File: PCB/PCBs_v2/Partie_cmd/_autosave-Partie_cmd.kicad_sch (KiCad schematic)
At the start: 54 parts, among them J1 Barrel_Jack, J2 Conn_01x04_Socket, J3 Conn_01x04_Socket, J4 Conn_01x11_Pin, J5 Conn_01x10_Pin, SW1 SW_MEC_5G, U1 ESP32-S3-DEVKITC-1-N8R2, U3 BU33SD5WG-TR, U4 XL1509-5.0

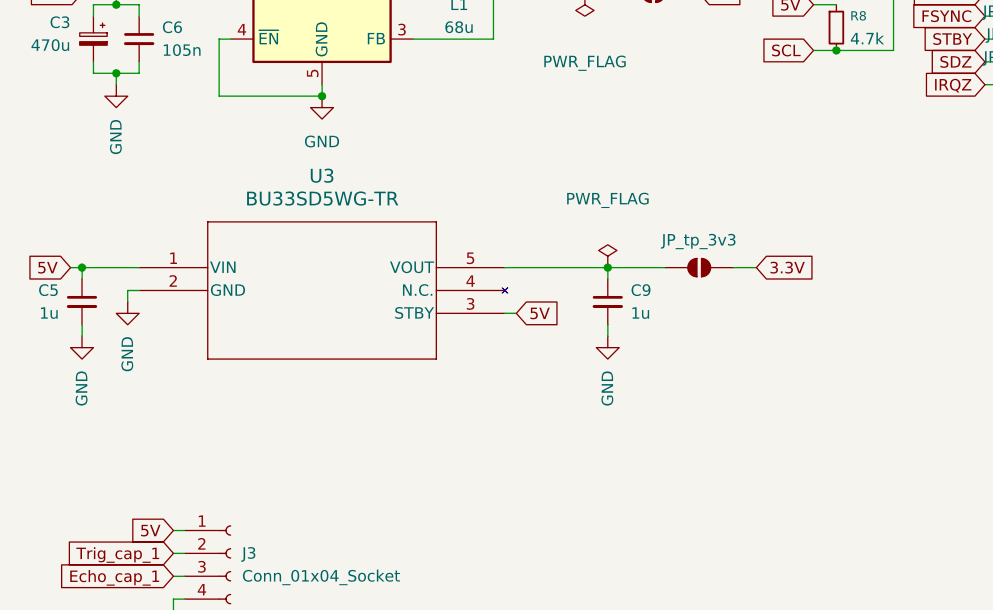
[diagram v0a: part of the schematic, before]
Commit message: pcb commande empruntes + debut routage
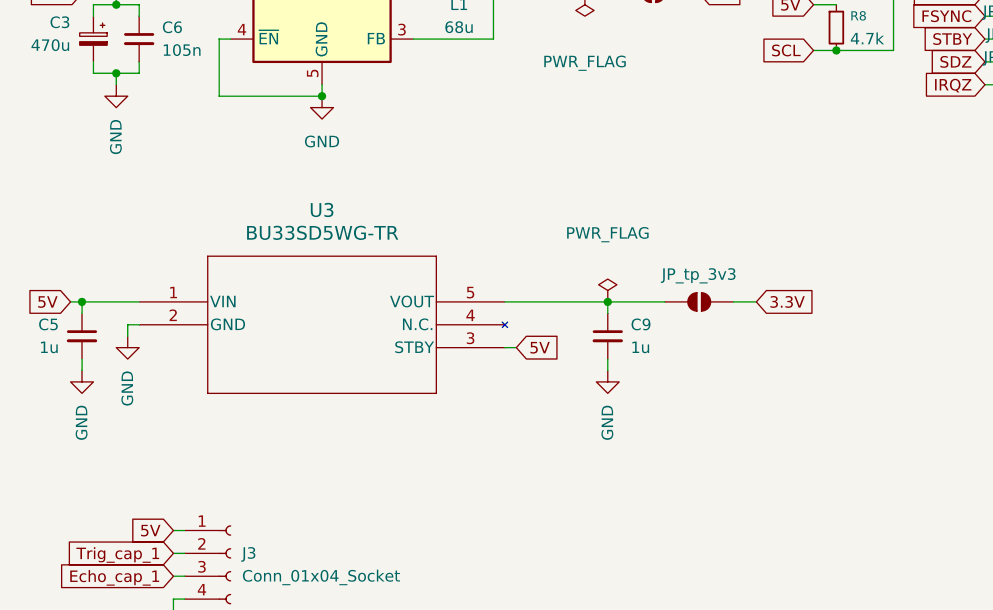
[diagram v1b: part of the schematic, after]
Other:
- moved on the sheet: C5, C9, JP_tp_3v3, U3
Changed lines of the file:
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@@
 	)
 	(junction
-		(at 40.64 99.06)
+		(at 40.64 102.87)
 		(diameter 0)
 		(color 0 0 0 0)
@@
 	)
 	(junction
-		(at 99.06 99.06)
+		(at 99.06 102.87)
 		(diameter 0)
 		(color 0 0 0 0)
@@
 	(wire
 		(pts
-			(xy 113.03 99.06) (xy 115.57 99.06)
+			(xy 113.03 102.87) (xy 115.57 102.87)
 		)
 		(stroke
@@
 	(wire
 		(pts
-			(xy 39.37 99.06) (xy 40.64 99.06)
+			(xy 39.37 102.87) (xy 40.64 102.87)
 		)
 		(stroke
@@
 	(wire
 		(pts
-			(xy 99.06 105.41) (xy 99.06 106.68)
+			(xy 99.06 109.22) (xy 99.06 110.49)
 		)
 		(stroke
@@
 	(wire
 		(pts
-			(xy 99.06 99.06) (xy 99.06 100.33)
+			(xy 99.06 102.87) (xy 99.06 104.14)
 		)
 		(stroke
@@
 	(wire
 		(pts
-			(xy 40.64 105.41) (xy 40.64 106.68)
+			(xy 40.64 109.22) (xy 40.64 110.49)
 		)
 		(stroke
@@
 	(wire
 		(pts
-			(xy 87.63 104.14) (xy 88.9 104.14)
+			(xy 87.63 107.95) (xy 88.9 107.95)
 		)
 		(stroke
@@
 	(wire
 		(pts
-			(xy 99.06 99.06) (xy 105.41 99.06)
+			(xy 99.06 102.87) (xy 105.41 102.87)
 		)
 		(stroke
@@
 	(wire
 		(pts
-			(xy 45.72 102.87) (xy 45.72 101.6)
+			(xy 45.72 106.68) (xy 45.72 105.41)
 		)
 		(stroke
@@
 	(wire
 		(pts
-			(xy 45.72 101.6) (xy 46.99 101.6)
+			(xy 45.72 105.41) (xy 46.99 105.41)
 		)
 		(stroke
@@
 	(wire
 		(pts
-			(xy 46.99 99.06) (xy 40.64 99.06)
+			(xy 46.99 102.87) (xy 40.64 102.87)
 		)
 		(stroke
@@
 	(wire
 		(pts
-			(xy 40.64 99.06) (xy 40.64 100.33)
+			(xy 40.64 102.87) (xy 40.64 104.14)
 		)
 		(stroke
@@
 	(wire
 		(pts
-			(xy 87.63 99.06) (xy 99.06 99.06)
+			(xy 87.63 102.87) (xy 99.06 102.87)
 		)
 		(stroke
@@
 	(global_label "5V"
 		(shape input)
-		(at 88.9 104.14 0)
+		(at 88.9 107.95 0)
 		(fields_autoplaced yes)
 		(effects
@@
 		)
 		(property "Intersheetrefs" "${INTERSHEET_REFS}"
-			(at 94.1833 104.14 0)
+			(at 94.1833 107.95 0)
 			(effects
 				(font
@@
 	(global_label "5V"
 		(shape input)
-		(at 39.37 99.06 180)
+		(at 39.37 102.87 180)
 		(fields_autoplaced yes)
 		(effects
@@
 		)
 		(property "Intersheetrefs" "${INTERSHEET_REFS}"
-			(at 34.0867 99.06 0)
+			(at 34.0867 102.87 0)
 			(effects
 				(font
@@
 	(global_label "3.3V"
 		(shape input)
-		(at 115.57 99.06 0)
+		(at 115.57 102.87 0)
 		(fields_autoplaced yes)
 		(effects
@@
 		)
 		(property "Intersheetrefs" "${INTERSHEET_REFS}"
-			(at 122.6676 99.06 0)
+			(at 122.6676 102.87 0)
 			(effects
 				(font
@@
 	(symbol
 		(lib_id "2025-09-19_12-39-26:BU33SD5WG-TR")
-		(at 46.99 99.06 0)
+		(at 46.99 102.87 0)
 		(unit 1)
 		(exclude_from_sim no)
@@
 		(fields_autoplaced yes)
 		(property "Reference" "U3"
-			(at 67.31 88.9 0)
+			(at 67.31 92.71 0)
 			(effects
 				(font
@@
 		)
 		(property "Value" "BU33SD5WG-TR"
-			(at 67.31 91.44 0)
+			(at 67.31 95.25 0)
 			(effects
 				(font
@@
 		)
 		(property "Footprint" "footprints:SSOP5_ROM-L"
-			(at 46.99 99.06 0)
+			(at 46.99 102.87 0)
 			(effects
 				(font
@@
 		)
 		(property "Datasheet" "BU33SD5WG-TR"
-			(at 46.99 99.06 0)
+			(at 46.99 102.87 0)
 			(effects
 				(font
@@
 		)
 		(property "Description" ""
-			(at 46.99 99.06 0)
+			(at 46.99 102.87 0)
 			(effects
 				(font
@@
 	(symbol
 		(lib_id "Device:C_Small")
-		(at 99.06 102.87 0)
+		(at 99.06 106.68 0)
 		(unit 1)
 		(exclude_from_sim no)
@@
 		(fields_autoplaced yes)
 		(property "Reference" "C9"
-			(at 101.6 101.6062 0)
+			(at 101.6 105.4162 0)
 			(effects
 				(font
@@
 		)
 		(property "Value" "1u"
-			(at 101.6 104.1462 0)
+			(at 101.6 107.9562 0)
 			(effects
 				(font
@@
 		)
 		(property "Footprint" "Capacitor_SMD:C_0603_1608Metric_Pad1.08x0.95mm_HandSolder"
-			(at 99.06 102.87 0)
+			(at 99.06 106.68 0)
 			(effects
 				(font
@@
 		)
 		(property "Datasheet" "~"
-			(at 99.06 102.87 0)
+			(at 99.06 106.68 0)
 			(effects
 				(font
@@
 		)
 		(property "Description" "Unpolarized capacitor, small symbol"
-			(at 99.06 102.87 0)
+			(at 99.06 106.68 0)
 			(effects
 				(font
@@
 	(symbol
 		(lib_id "power:PWR_FLAG")
-		(at 99.06 99.06 0)
+		(at 99.06 102.87 0)
 		(unit 1)
 		(exclude_from_sim no)
@@
 		(dnp no)
 		(property "Reference" "#FLG03"
-			(at 99.06 97.155 0)
+			(at 99.06 100.965 0)
 			(effects
 				(font
@@
 		)
 		(property "Value" "PWR_FLAG"
-			(at 99.06 91.44 0)
+			(at 99.06 95.25 0)
 			(effects
 				(font
@@
 		)
 		(property "Footprint" ""
-			(at 99.06 99.06 0)
+			(at 99.06 102.87 0)
 			(effects
 				(font
@@
 		)
 		(property "Datasheet" "~"
-			(at 99.06 99.06 0)
+			(at 99.06 102.87 0)
 			(effects
 				(font
@@
 		)
 		(property "Description" "Special symbol for telling ERC where power comes from"
-			(at 99.06 99.06 0)
+			(at 99.06 102.87 0)
 			(effects
 				(font
@@
 	(symbol
 		(lib_id "Jumper:SolderJumper_2_Open")
-		(at 109.22 99.06 0)
+		(at 109.22 102.87 0)
 		(unit 1)
 		(exclude_from_sim no)
@@
 		(dnp no)
 		(property "Reference" "JP_tp_3v3"
-			(at 109.22 96.012 0)
+			(at 109.22 99.822 0)
 			(effects
 				(font
@@
 		)
 		(property "Value" "SolderJumper_2_Open"
-			(at 109.22 95.25 0)
+			(at 109.22 99.06 0)
 			(effects
 				(font
@@
 		)
 		(property "Footprint" "Jumper:SolderJumper-2_P1.3mm_Open_TrianglePad1.0x1.5mm"
-			(at 109.22 99.06 0)
+			(at 109.22 102.87 0)
 			(effects
 				(font
@@
 		)
 		(property "Datasheet" "~"
-			(at 109.22 99.06 0)
+			(at 109.22 102.87 0)
 			(effects
 				(font
@@
 		)
 		(property "Description" "Solder Jumper, 2-pole, open"
-			(at 109.22 99.06 0)
+			(at 109.22 102.87 0)
 			(effects
 				(font
@@
 	(symbol
 		(lib_id "Device:C_Small")
-		(at 40.64 102.87 0)
+		(at 40.64 106.68 0)
 		(mirror y)
 		(unit 1)
@@
 		(dnp no)
 		(property "Reference" "C5"
-			(at 38.1 101.6062 0)
+			(at 38.1 105.4162 0)
 			(effects
 				(font
@@
 		)
 		(property "Value" "1u"
-			(at 38.1 104.1462 0)
+			(at 38.1 107.9562 0)
 			(effects
 				(font
@@
 		)
 		(property "Footprint" "Capacitor_SMD:C_0603_1608Metric_Pad1.08x0.95mm_HandSolder"
-			(at 40.64 102.87 0)
+			(at 40.64 106.68 0)
 			(effects
 				(font
@@
 		)
 		(property "Datasheet" "~"
-			(at 40.64 102.87 0)
+			(at 40.64 106.68 0)
 			(effects
 				(font
@@
 		)
 		(property "Description" "Unpolarized capacitor, small symbol"
-			(at 40.64 102.87 0)
+			(at 40.64 106.68 0)
 			(effects
 				(font
@@
 	(symbol
 		(lib_id "power:GND")
-		(at 45.72 102.87 0)
+		(at 45.72 106.68 0)
 		(unit 1)
 		(exclude_from_sim no)
@@
 		(fields_autoplaced yes)
 		(property "Reference" "#PWR08"
-			(at 45.72 109.22 0)
+			(at 45.72 113.03 0)
 			(effects
 				(font
@@
 		)
 		(property "Value" "GND"
-			(at 45.7201 106.68 90)
+			(at 45.7201 110.49 90)
 			(effects
 				(font
@@
 		)
 		(property "Footprint" ""
-			(at 45.72 102.87 0)
+			(at 45.72 106.68 0)
 			(effects
 				(font
@@
 		)
 		(property "Datasheet" ""
-			(at 45.72 102.87 0)
+			(at 45.72 106.68 0)
 			(effects
 				(font
@@
 		)
 		(property "Description" "Power symbol creates a global label with name \"GND\" , ground"
-			(at 45.72 102.87 0)
+			(at 45.72 106.68 0)
 			(effects
 				(font
@@
 	(symbol
 		(lib_id "power:GND")
-		(at 99.06 106.68 0)
+		(at 99.06 110.49 0)
 		(unit 1)
 		(exclude_from_sim no)
@@
 		(fields_autoplaced yes)
 		(property "Reference" "#PWR013"
-			(at 99.06 113.03 0)
+			(at 99.06 116.84 0)
 			(effects
 				(font
@@
 		)
 		(property "Value" "GND"
-			(at 99.0601 110.49 90)
+			(at 99.0601 114.3 90)
 			(effects
 				(font
@@
 		)
 		(property "Footprint" ""
-			(at 99.06 106.68 0)
+			(at 99.06 110.49 0)
 			(effects
 				(font
@@
 		)
 		(property "Datasheet" ""
-			(at 99.06 106.68 0)
+			(at 99.06 110.49 0)
 			(effects
 				(font
@@
 		)
 		(property "Description" "Power symbol creates a global label with name \"GND\" , ground"
-			(at 99.06 106.68 0)
+			(at 99.06 110.49 0)
 			(effects
 				(font
@@
 	(symbol
 		(lib_id "power:GND")
-		(at 40.64 106.68 0)
+		(at 40.64 110.49 0)
 		(unit 1)
 		(exclude_from_sim no)
@@
 		(fields_autoplaced yes)
 		(property "Reference" "#PWR05"
-			(at 40.64 113.03 0)
+			(at 40.64 116.84 0)
 			(effects
 				(font
@@
 		)
 		(property "Value" "GND"
-			(at 40.6401 110.49 90)
+			(at 40.6401 114.3 90)
 			(effects
 				(font
@@
 		)
 		(property "Footprint" ""
-			(at 40.64 106.68 0)
+			(at 40.64 110.49 0)
 			(effects
 				(font
@@
 		)
 		(property "Datasheet" ""
-			(at 40.64 106.68 0)
+			(at 40.64 110.49 0)
 			(effects
 				(font
@@
 		)
 		(property "Description" "Power symbol creates a global label with name \"GND\" , ground"
-			(at 40.64 106.68 0)
+			(at 40.64 110.49 0)
 			(effects
 				(font
